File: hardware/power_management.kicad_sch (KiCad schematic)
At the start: 8 parts, among them J3 Conn_01x02, Q1 IRLML6402, U2 BMS Module

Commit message: Electric Rules Check completed.
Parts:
- D3: symbol Diode:PMEG4010CEJ -> kitchen_timer-symbols_lib:PMEG4010CEJ
- U2: value BMS Module -> TP4056 breakout; symbol kitchen_timer-symbols_lib:BMS_Module -> kitchen_timer-symbols_lib:TP4056 breakout; now in the parts list
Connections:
- net BAT+: now also U2.4 (B+); no longer U2.3 (B+)
- net BAT-: now also U2.5 (B-); no longer U2.4 (B-)
- net GND-USB renamed GND
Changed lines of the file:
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@@
 		)
 	)
-	(hierarchical_label "GND-USB"
+	(global_label "GND"
 		(shape input)
 		(at 166.37 110.49 180)
+		(fields_autoplaced yes)
 		(effects
 			(font
@@
 			)
 			(justify right)
+		)
+		(property "Intersheetrefs" "${INTERSHEET_REFS}"
+			(at 159.5143 110.49 0)
+			(effects
+				(font
+					(size 1.27 1.27)
+				)
+				(justify right)
+				(hide yes)
+			)
+		)
+	)
+	(global_label "GND"
+		(shape input)
+		(at 92.71 113.03 180)
+		(fields_autoplaced yes)
+		(effects
+			(font
+				(size 1.27 1.27)
+			)
+			(justify right)
+		)
+		(property "Intersheetrefs" "${INTERSHEET_REFS}"
+			(at 85.8543 113.03 0)
+			(effects
+				(font
+					(size 1.27 1.27)
+				)
+				(justify right)
+				(hide yes)
+			)
 		)
 	)
@@
 		)
 	)
-	(hierarchical_label "PP_GND"
+	(hierarchical_label "GND"
 		(shape output)
 		(at 200.66 110.49 0)
@@
 		)
 	)
-	(hierarchical_label "GND-USB"
-		(shape input)
-		(at 92.71 113.03 180)
-		(effects
-			(font
-				(size 1.27 1.27)
-			)
-			(justify right)
-		)
-	)
 	(symbol
-		(lib_id "Diode:PMEG4010CEJ")
+		(lib_id "kitchen_timer-symbols_lib:PMEG4010CEJ")
 		(at 190.5 101.6 180)
 		(unit 1)
@@
 	)
 	(symbol
-		(lib_id "kitchen_timer-symbols_lib:BMS_Module")
+		(lib_id "kitchen_timer-symbols_lib:TP4056 breakout")
 		(at 106.68 111.76 0)
 		(unit 1)
 		(exclude_from_sim no)
-		(in_bom no)
+		(in_bom yes)
 		(on_board yes)
 		(dnp no)
 		(property "Reference" "U2"
-			(at 100.33 103.886 0)
-			(effects
-				(font
-					(size 1.27 1.27)
-				)
-			)
-		)
-		(property "Value" "BMS Module"
-			(at 108.204 119.634 0)
+			(at 99.822 104.394 0)
+			(effects
+				(font
+					(size 1.27 1.27)
+					(thickness 0.1588)
+				)
+			)
+		)
+		(property "Value" "TP4056 breakout"
+			(at 107.188 119.888 0)
 			(effects
 				(font
@@
 			)
 		)
-		(property "Description" "TP4056 laddare med skyddskrets för Li-Ion- och LiPo-cell"
+		(property "Description" "TP4056 charger with protection for Li-Ion and LiPo cell"
 			(at 106.68 113.03 0)
 			(effects

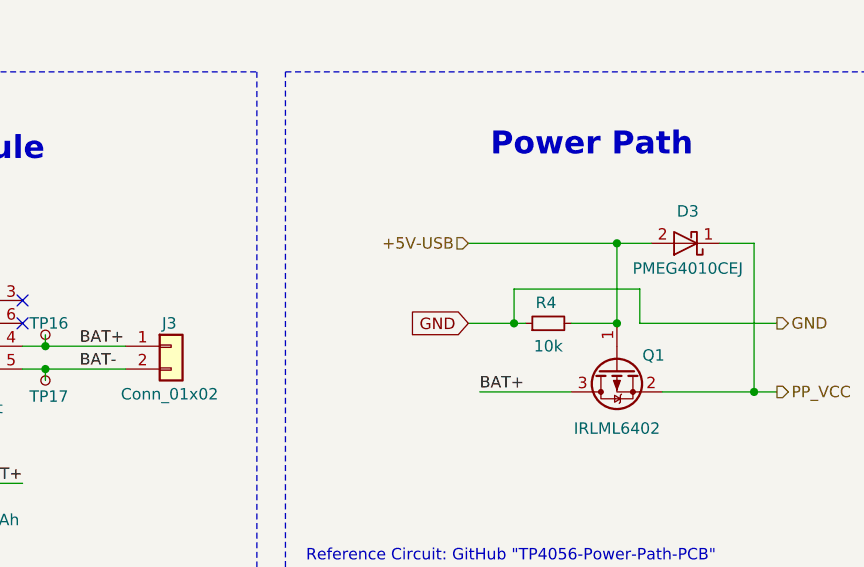
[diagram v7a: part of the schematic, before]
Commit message: Added footprints to mounting holes and selected a part for the test LED.
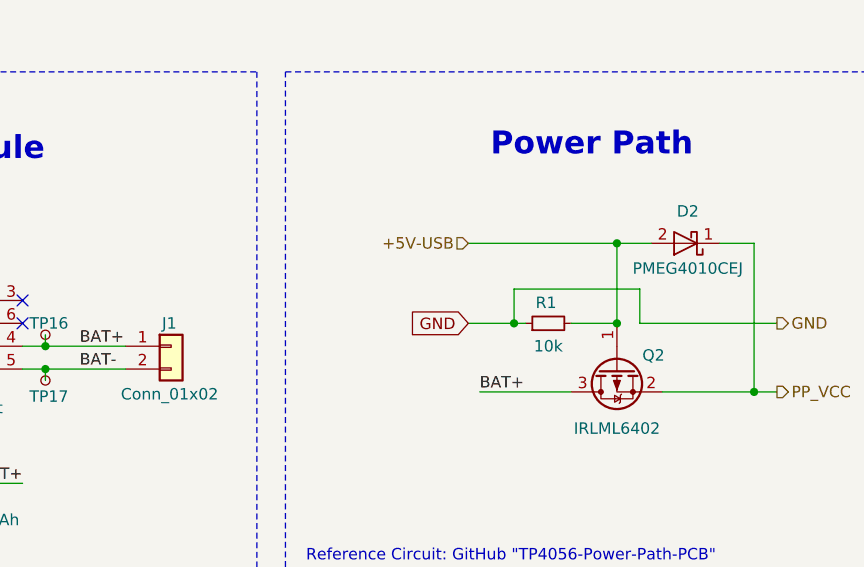
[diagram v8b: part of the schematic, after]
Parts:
- renumbered D3 to D2, J3 to J1, Q1 to Q2, R4 to R1
